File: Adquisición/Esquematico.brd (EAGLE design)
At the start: 32 x 20.6 mm, 9 parts, among them IC1 LM358N

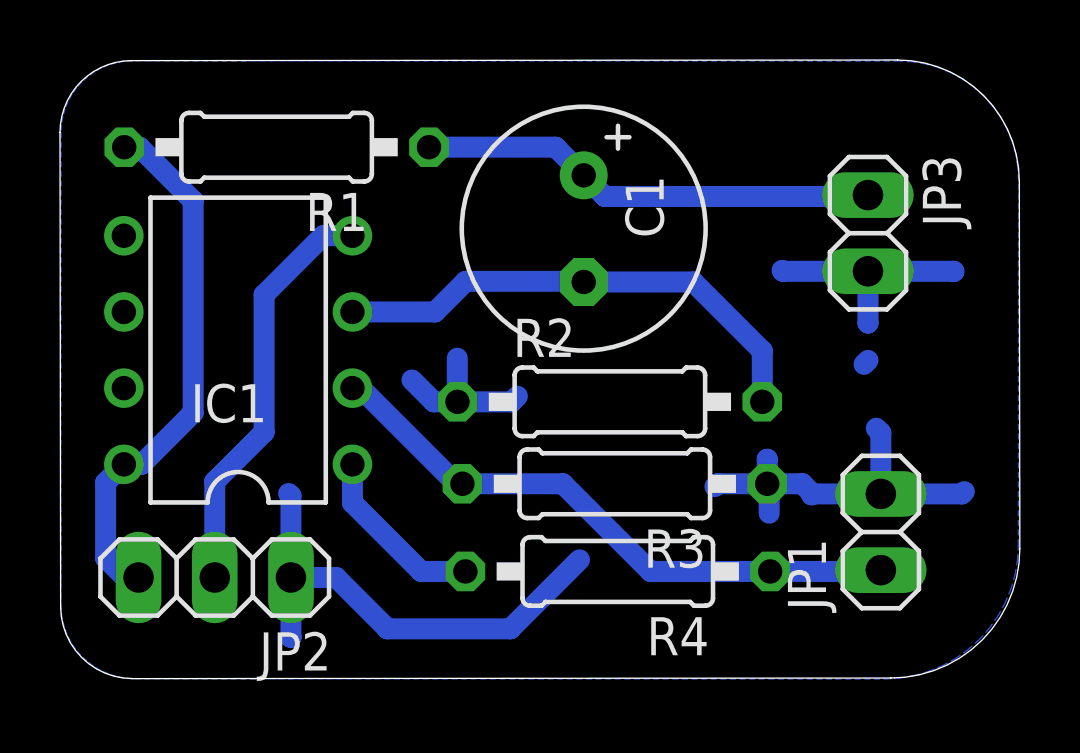
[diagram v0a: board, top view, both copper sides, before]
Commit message: Se agregan pistas para los filtros y se crean los comparadores
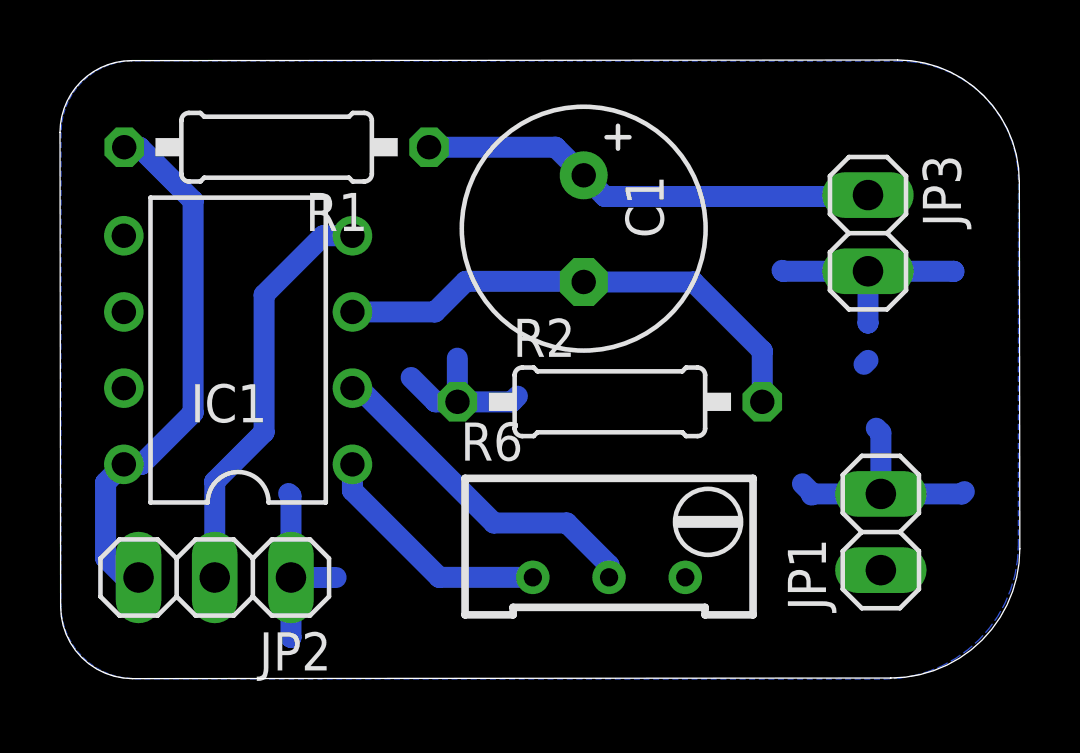
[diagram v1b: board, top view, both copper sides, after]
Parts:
- removed R3: 10k, rcl:0207/10
- removed R4: 33k, rcl:0207/10
- added R6: (no value), rcl:RTRIM64W
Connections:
- removed net N$5: IC1.1, R4.2
- new net N$2: IC1.2, R6.2
- net 0: now also R6.3; no longer R3.1
- net VAMP: now also IC1.1, R6.1; no longer IC1.2, R3.2, R4.1
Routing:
- net 0: track 41.8 -> 27.3 mm
- net VAMP: track 20.2 -> 8.15 mm
- net N$2: track 0.00 -> 11.4 mm
- net N$5: track 5.99 -> 0.00 mm
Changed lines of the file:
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@@
 <drawing>
 <settings>
-<setting alwaysvectorfont="yes"/>
+<setting alwaysvectorfont="no"/>
 <setting verticaltext="up"/>
 </settings>
@@
 <attribute name="VALUE" x="16.044015625" y="8.59358125" size="1.27" layer="27" ratio="10"/>
 </element>
-<element name="R3" library="rcl" library_urn="urn:adsk.eagle:library:334" package="0207/10" package3d_urn="urn:adsk.eagle:package:23491/2" value="10k" x="18.469478125" y="6.4973125" smashed="yes" rot="R180">
-<attribute name="NAME" x="21.517478125" y="4.9733125" size="1.27" layer="25" ratio="10" rot="R180"/>
-<attribute name="POPULARITY" value="36" x="-0.580521875" y="53.4873125" size="1.778" layer="27" rot="R180" display="off"/>
-<attribute name="SPICEPREFIX" value="R" x="-0.580521875" y="53.4873125" size="1.778" layer="27" rot="R180" display="off"/>
-<attribute name="VALUE" x="20.730078125" y="7.1323125" size="1.27" layer="27" ratio="10" rot="R180"/>
-</element>
-<element name="R4" library="rcl" library_urn="urn:adsk.eagle:library:334" package="0207/10" package3d_urn="urn:adsk.eagle:package:23491/2" value="33k" x="18.567934375" y="3.574821875" smashed="yes" rot="R180">
-<attribute name="NAME" x="21.615934375" y="2.050821875" size="1.27" layer="25" ratio="10" rot="R180"/>
-<attribute name="POPULARITY" value="36" x="-13.182065625" y="50.564821875" size="1.778" layer="27" rot="R180" display="off"/>
-<attribute name="SPICEPREFIX" value="R" x="-13.182065625" y="50.564821875" size="1.778" layer="27" rot="R180" display="off"/>
-<attribute name="VALUE" x="20.828534375" y="4.209821875" size="1.27" layer="27" ratio="10" rot="R180"/>
-</element>
 <element name="JP1" library="pinhead" library_urn="urn:adsk.eagle:library:325" package="1X02" package3d_urn="urn:adsk.eagle:package:22435/2" value="" x="27.33705625" y="4.8883125" smashed="yes" rot="R90">
 <attribute name="NAME" x="25.50825625" y="2.2721125" size="1.27" layer="25" ratio="10" rot="R90"/>
@@
 <attribute name="POPULARITY" value="98" x="26.90845" y="14.85025" size="1.778" layer="27" rot="R270" display="off"/>
 <attribute name="VALUE" x="23.73345" y="17.39025" size="1.27" layer="27" rot="R270"/>
+</element>
+<element name="R6" library="rcl" library_urn="urn:adsk.eagle:library:334" package="RTRIM64W" package3d_urn="urn:adsk.eagle:package:23748/1" value="" x="18.277440625" y="4.6478375" smashed="yes" rot="R270">
+<attribute name="NAME" x="13.327440625" y="7.2678375" size="1.27" layer="25"/>
+<attribute name="POPULARITY" value="0" x="18.277440625" y="4.6478375" size="1.778" layer="27" rot="R270" display="off"/>
+<attribute name="SPICEMODEL" value="X" x="18.277440625" y="4.6478375" size="1.778" layer="27" rot="R270" display="off"/>
+<attribute name="SPICEPREFIXL" value="POT" x="18.277440625" y="4.6478375" size="1.778" layer="27" rot="R270" display="off"/>
+<attribute name="VALUE" x="13.327440625" y="0.2978375" size="1.27" layer="27"/>
 </element>
 </elements>
@@
 </signal>
 <signal name="VAMP">
-<contactref element="IC1" pad="2"/>
-<contactref element="R3" pad="2"/>
-<contactref element="R4" pad="1"/>
 <contactref element="JP1" pad="1"/>
-<wire x1="13.186871875" y1="6.4973125" x2="9.999415625" y2="9.68476875" width="0.7" layer="16"/>
-<wire x1="9.72339375" y1="9.68476875" x2="9.999415625" y2="9.68476875" width="0.7" layer="16"/>
-<wire x1="13.186871875" y1="6.4973125" x2="13.389478125" y2="6.4973125" width="0.7" layer="16"/>
-<wire x1="19.660553125" y1="3.574821875" x2="16.7380625" y2="6.4973125" width="0.7" layer="16"/>
-<wire x1="13.389478125" y1="6.4973125" x2="16.7380625" y2="6.4973125" width="0.7" layer="16"/>
-<wire x1="19.660553125" y1="3.574821875" x2="23.647934375" y2="3.574821875" width="0.7" layer="16"/>
-<wire x1="23.647934375" y1="3.574821875" x2="27.293565625" y2="3.574821875" width="0.7" layer="16"/>
 <wire x1="27.293565625" y1="3.574821875" x2="27.33705625" y2="3.6183125" width="0.7" layer="16"/>
-</signal>
-<signal name="N$5">
 <contactref element="IC1" pad="1"/>
-<contactref element="R4" pad="2"/>
-<wire x1="12.01459375" y1="3.574821875" x2="9.72339375" y2="5.866021875" width="0.7" layer="16"/>
-<wire x1="9.72339375" y1="7.14476875" x2="9.72339375" y2="5.866021875" width="0.7" layer="16"/>
-<wire x1="12.01459375" y1="3.574821875" x2="13.487934375" y2="3.574821875" width="0.7" layer="16"/>
+<contactref element="R6" pad="1"/>
+<wire x1="12.616046875" y1="3.3778375" x2="9.72339375" y2="6.270490625" width="0.7" layer="16"/>
+<wire x1="9.72339375" y1="7.14476875" x2="9.72339375" y2="6.270490625" width="0.7" layer="16"/>
+<wire x1="12.616046875" y1="3.3778375" x2="15.737440625" y2="3.3778375" width="0.7" layer="16"/>
+<wire x1="15.737440625" y1="3.3778375" x2="27.293565625" y2="3.574821875" width="0" layer="19" extent="16-16"/>
 </signal>
 <signal name="V-">
@@
 </signal>
 <signal name="0">
-<contactref element="R3" pad="1"/>
 <contactref element="R2" pad="1"/>
 <polygon width="0" layer="16">
@@
 <contactref element="JP3" pad="2"/>
 <wire x1="7.673621875" y1="3.37284375" x2="9.1794" y2="3.37284375" width="0.7" layer="16"/>
-<wire x1="10.891025" y1="1.66121875" x2="14.98941875" y2="1.66121875" width="0.7" layer="16"/>
-<wire x1="14.98941875" y1="1.66121875" x2="17.2918375" y2="3.9636375" width="0.7" layer="16"/>
-<wire x1="9.1794" y1="3.37284375" x2="10.891025" y2="1.66121875" width="0.7" layer="16"/>
 <wire x1="26.90845" y1="10.611059375" x2="26.77546875" y2="10.478078125" width="0.7" layer="16"/>
 <wire x1="27.33705625" y1="6.1583125" x2="27.33705625" y2="8.19691875" width="0.7" layer="16"/>
@@
 <wire x1="13.224615625" y1="9.22858125" x2="13.2193" y2="9.233896875" width="0.7" layer="16"/>
 <wire x1="13.2193" y1="9.233896875" x2="13.2193" y2="10.68301875" width="0.7" layer="16"/>
-<wire x1="13.224615625" y1="9.22858125" x2="12.435509375" y2="9.22858125" width="0.7" layer="16"/>
-<wire x1="12.435509375" y1="9.22858125" x2="11.706403125" y2="9.9576875" width="0.7" layer="16"/>
+<wire x1="13.224615625" y1="9.22858125" x2="12.490290625" y2="9.22858125" width="0.7" layer="16"/>
+<wire x1="12.490290625" y1="9.22858125" x2="11.679028125" y2="10.03984375" width="0.7" layer="16"/>
 <wire x1="27.33705625" y1="6.1583125" x2="25.062459375" y2="6.1583125" width="0.7" layer="16"/>
 <wire x1="25.062459375" y1="6.1583125" x2="25.02510625" y2="6.120959375" width="0.7" layer="16"/>
@@
 <wire x1="26.90845" y1="13.58025" x2="26.90845" y2="11.854775" width="0.7" layer="16"/>
 <wire x1="26.90845" y1="11.854775" x2="26.9093125" y2="11.8539125" width="0.7" layer="16"/>
-<wire x1="23.549478125" y1="6.4973125" x2="21.89951875" y2="6.4973125" width="0.7" layer="16"/>
-<wire x1="21.89951875" y1="6.4973125" x2="21.80586875" y2="6.4036625" width="0.7" layer="16"/>
-<wire x1="23.549478125" y1="6.4973125" x2="24.723459375" y2="6.4973125" width="0.7" layer="16"/>
 <wire x1="24.723459375" y1="6.4973125" x2="25.062459375" y2="6.1583125" width="0.7" layer="16"/>
-<wire x1="23.549478125" y1="6.4973125" x2="23.615009375" y2="6.43178125" width="0.7" layer="16"/>
-<wire x1="23.615009375" y1="6.43178125" x2="23.615009375" y2="5.515028125" width="0.7" layer="16"/>
-<wire x1="23.549478125" y1="6.4973125" x2="23.549478125" y2="7.313571875" width="0.7" layer="16"/>
-<wire x1="23.549478125" y1="7.313571875" x2="23.5508875" y2="7.31498125" width="0.7" layer="16"/>
+<contactref element="R6" pad="3"/>
 </signal>
 <signal name="VO">
@@
 <wire x1="23.384615625" y1="10.925590625" x2="23.384615625" y2="9.22858125" width="0.7" layer="16"/>
 </signal>
+<signal name="N$2">
+<contactref element="IC1" pad="2"/>
+<contactref element="R6" pad="2"/>
+<wire x1="18.277440625" y1="3.7837" x2="18.277440625" y2="3.3778375" width="0.7" layer="16"/>
+<wire x1="18.277440625" y1="3.7837" x2="16.87130625" y2="5.189834375" width="0.7" layer="16"/>
+<wire x1="14.43735625" y1="5.189834375" x2="16.87130625" y2="5.189834375" width="0.7" layer="16"/>
+<wire x1="9.72339375" y1="9.68476875" x2="9.942421875" y2="9.68476875" width="0.7" layer="16"/>
+<wire x1="14.43735625" y1="5.189834375" x2="9.942421875" y2="9.68476875" width="0.7" layer="16"/>
+</signal>
 </signals>
